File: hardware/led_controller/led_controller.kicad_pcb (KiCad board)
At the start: 2 copper layers, 50 x 70 mm, 32 parts, among them J1 Header, J2 Header, J3 Header, J4 Header, J5 POWER, J6 Conn_01x02, U1 74AHCT125, U3 Waveshare ESP32-S3/C6 Zero

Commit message: PCB updates + fudicials fix
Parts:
- added J7: Conn_01x06_Pin, Connector_PinHeader_2.54mm:PinHeader_1x06_P2.54mm_Vertical, F.Cu at (164.1, 73.9)
- moved D2 7.76 mm to (164.3, 83.1)
- moved C9 4.88 mm to (158.4, 79.0)
- moved FID2 4.03 mm to (163.5, 57.5)
- moved R5 0.35 mm to (154.1, 77.7)
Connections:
- C9 pad 1: Net-(D2-A) -> Net-(C9-Pad1)
- R5 pad 1: Net-(D2-A) -> Net-(C9-Pad1)
- U3 pad 11: unconnected-(U3-S3_GPIO8/C6_GPIO21-Pad11)_1 -> IO1
- U3 pad 12: unconnected-(U3-S3_GPIO9/C6_GPIO20-Pad12)_1 -> IO2
- U3 pad 17: unconnected-(U3-S3_GPIO44_RX/C6_RX-Pad17)_1 -> IO3/RX
- U3 pad 18: unconnected-(U3-S3_GPIO43_TX/C6_TX-Pad18) -> IO4/TX
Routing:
- net +5V: track 133.8 -> 163.1 mm
- net IO4/TX: track 0.00 -> 12.9 mm
- net IO3/RX: track 0.00 -> 12.9 mm
- net Net-(D2-K): track 15.6 -> 7.88 mm
- net IO2: track 0.00 -> 6.33 mm
- net IO1: track 0.00 -> 6.31 mm
- net Net-(C9-Pad1): track 0.00 -> 2.92 mm
- net Net-(D2-A): track 11.3 -> 12.2 mm
- net +3.3V: track 26.4 -> 27.1 mm, vias 1 -> 2
- net +4.6V: track 48.9 -> 49.5 mm, vias 1 -> 2
- net GND: vias 14 -> 24
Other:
- board text added: "3V3"
- board text added: "IO1"
- board text added: "IO2"
- board text added: "IO3"

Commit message: Tuning layout
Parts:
- moved FID2 28.7 mm to (167.0, 86.0)
- moved FID3 19.9 mm to (132.5, 114.5)
- moved FID1 9.90 mm to (129.5, 54.5)
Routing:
- added copper zone on F.Cu, net +5V
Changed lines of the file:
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@@
 	(footprint "Fiducial:Fiducial_1mm_Mask2mm"
 		(layer "F.Cu")
-		(at 136.5 61.5)
+		(at 129.5 54.5)
 		(descr "Fiducial, circular marking, 1mm bare copper, 2mm soldermask opening (Level A)")
 		(tags "fiducial")
@@
 		(sheetname "/")
 		(sheetfile "led_controller.kicad_sch")
-		(units
-			(unit
-				(name "A")
-				(pins)
-			)
-		)
 		(attr smd exclude_from_bom)
 		(duplicate_pad_numbers_are_jumpers no)
@@
 	(footprint "Fiducial:Fiducial_1mm_Mask2mm"
 		(layer "F.Cu")
-		(at 163.5 57.5)
+		(at 167 86)
 		(descr "Fiducial, circular marking, 1mm bare copper, 2mm soldermask opening (Level A)")
 		(tags "fiducial")
@@
 	(footprint "Fiducial:Fiducial_1mm_Mask2mm"
 		(layer "F.Cu")
-		(at 136.5 95)
+		(at 132.5 114.5)
 		(descr "Fiducial, circular marking, 1mm bare copper, 2mm soldermask opening (Level A)")
 		(tags "fiducial")
@@
 		(sheetname "/")
 		(sheetfile "led_controller.kicad_sch")
-		(units
-			(unit
-				(name "A")
-				(pins)
-			)
-		)
 		(attr smd exclude_from_bom)
 		(duplicate_pad_numbers_are_jumpers no)
@@
 			(pinfunction "Pin_1_1")
 			(pintype "passive")
+			(zone_connect 2)
 		)
 		(pad "2" thru_hole circle
@@
 	)
 	(zone
+		(net "+5V")
+		(layer "F.Cu")
+		(hatch edge 0.5)
+		(priority 1)
+		(connect_pads
+			(clearance 0.1)
+		)
+		(min_thickness 0.25)
+		(fill yes
+			(thermal_gap 0.5)
+			(thermal_bridge_width 0.5)
+			(island_removal_mode 0)
+		)
+		(polygon
+			(pts
+				(xy 121.175 64) (xy 125 61.6) (xy 124.825 63) (xy 123.675 65.325)
+			)
+		)
+	)
+	(zone

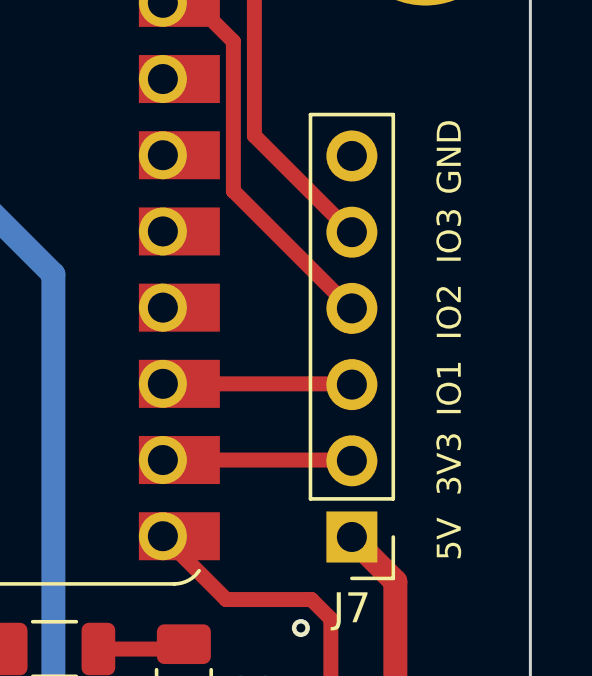
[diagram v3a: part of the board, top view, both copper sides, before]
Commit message: Incorrect labelling on IO port
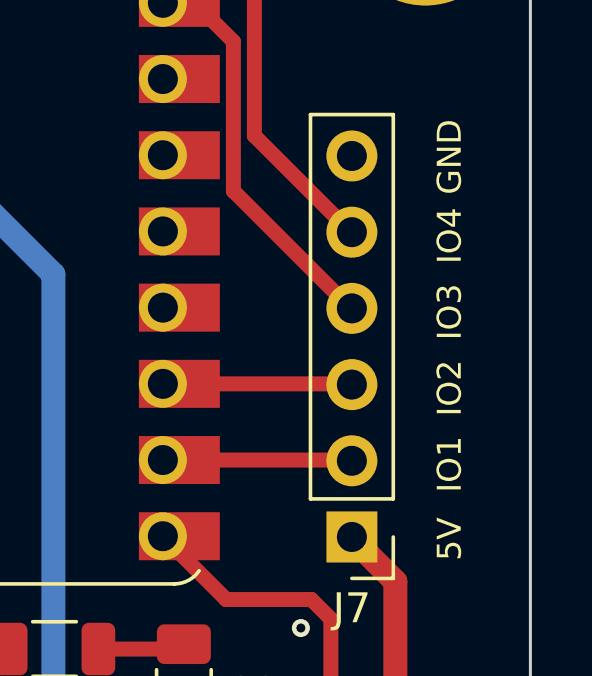
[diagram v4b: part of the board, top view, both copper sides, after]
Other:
- board text added: "IO4"
- board text removed: "3V3"
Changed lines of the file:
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@@
 			(pinfunction "Pin_6_6")
 			(pintype "passive")
+			(zone_connect 1)
 		)
 		(embedded_fonts no)
@@
 		)
 	)
-	(gr_text "IO3"
+	(gr_text "IO4"
 		(at 167.7765 64.815476 90)
 		(layer "F.SilkS")
@@
 		)
 	)
-	(gr_text "IO2"
+	(gr_text "IO3"
 		(at 167.7765 67.355476 90)
 		(layer "F.SilkS")
@@
 		)
 	)
-	(gr_text "IO1"
+	(gr_text "IO2"
 		(at 167.7765 69.895476 90)
 		(layer "F.SilkS")
@@
 		)
 	)
-	(gr_text "3V3"
-		(at 167.7765 72.549762 90)
+	(gr_text "IO1"
+		(at 167.7765 72.435476 90)
 		(layer "F.SilkS")
 		(effects

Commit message: Update version/date info
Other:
- board text added: "Aug 2026"
- board text added: "LED Controller V1.1"
- board text removed: "July 2026"
- board text removed: "LED Controller V1.0"

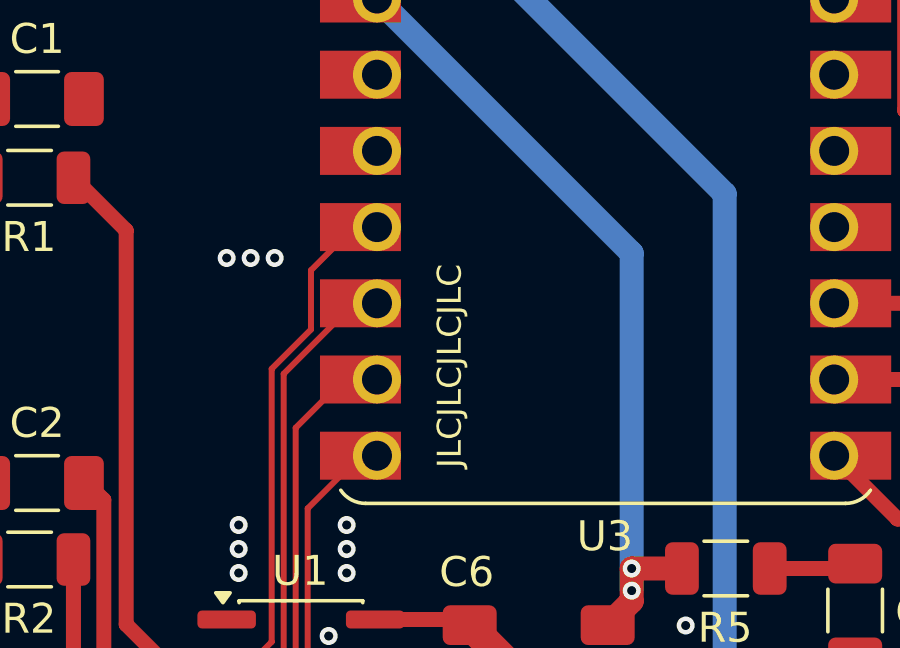
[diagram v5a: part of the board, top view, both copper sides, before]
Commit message: Set thermal relief constraints for top and bottom fill zones
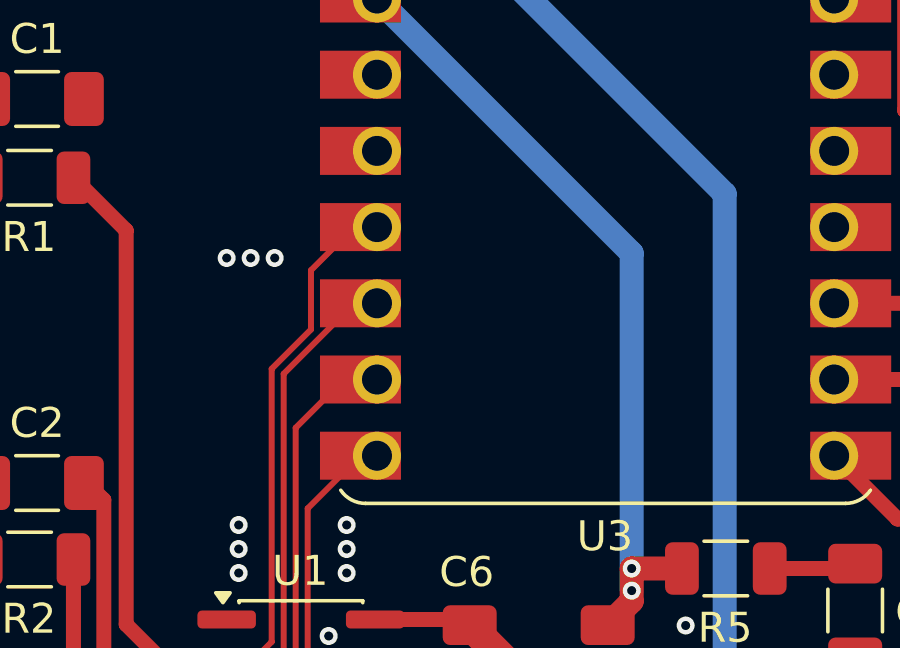
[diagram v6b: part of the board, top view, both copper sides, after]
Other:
- board text removed: "JLCJLCJLCJLC"
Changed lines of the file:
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@@
-		)
-	)
-	(gr_text "JLCJLCJLCJLC"
-		(at 145.4 74.3 90)
-		(layer "F.SilkS")
-		(effects
-			(font
-				(size 0.8 0.8)
-				(thickness 0.1)
-			)
-			(justify left bottom)
 		)
 	)
@@
 		(net "GND")
 		(layer "F.Cu")
-		(name "GND")
+		(name "GND_1")
 		(hatch edge 0.5)
 		(connect_pads
@@
 		(min_thickness 0.25)
 		(fill yes
-			(thermal_gap 0)
-			(thermal_bridge_width 0)
+			(thermal_gap 0.3)
+			(thermal_bridge_width 0.4)
 			(island_removal_mode 0)
 		)
@@
 		(min_thickness 0.25)
 		(fill yes
-			(thermal_gap 0)
-			(thermal_bridge_width 0)
+			(thermal_gap 0.3)
+			(thermal_bridge_width 0.4)
 			(island_removal_mode 0)
 		)
